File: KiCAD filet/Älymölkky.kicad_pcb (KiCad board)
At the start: 2 copper layers, 99 parts, among them P0.18_TP1 Conn_01x01_Male, U1 nRF52810-QCxx, X1 32MHz Crystal, X1_C1 12pF, X1_C2 12pF, X2 32.768 kHz Crystal, X2_C11 12pF, X2_C12 12pF

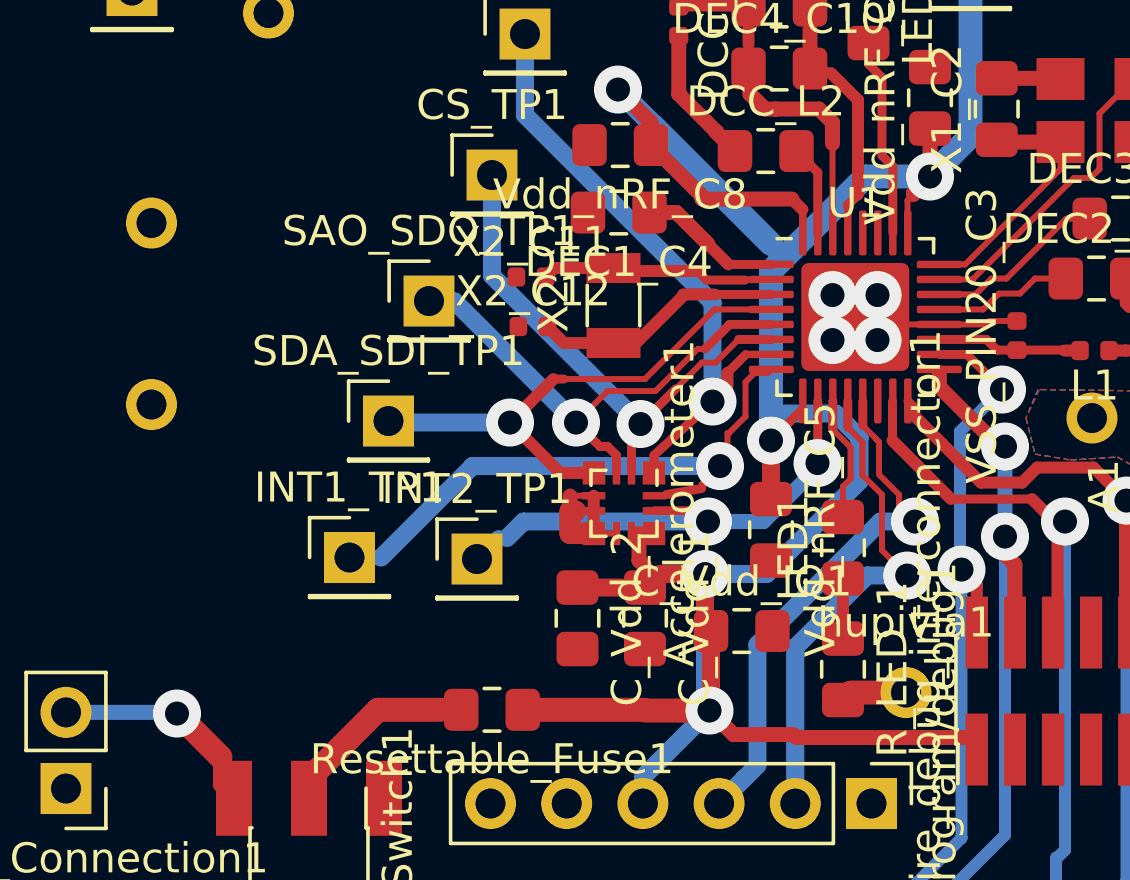
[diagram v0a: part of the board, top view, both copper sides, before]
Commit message: Modified some traces, larger size capacitors on crystal
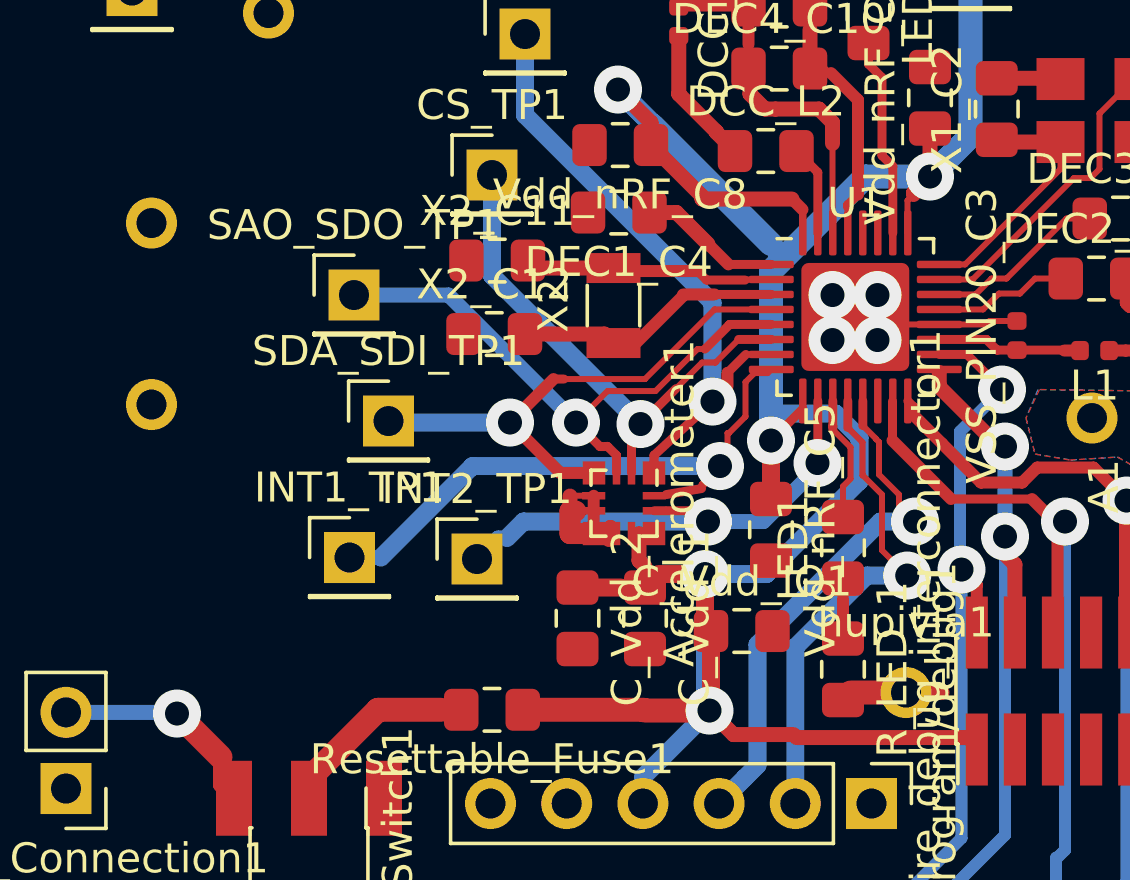
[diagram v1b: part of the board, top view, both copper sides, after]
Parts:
- X2_C11, X2_C12: footprint Capacitor_SMD:C_0402_1005Metric -> Capacitor_SMD:C_0805_2012Metric_Pad1.15x1.40mm_HandSolder
- moved SAO_SDO_TP1 2.51 mm to (114.1, 93.2)
- moved X2_C12 1.31 mm to (118.8, 94.5)
- moved X2_C11 1.25 mm to (118.9, 92.1)
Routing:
- net /~SAO_SDO: track 17.1 -> 19.6 mm
- net Earth: track 34.4 -> 36.6 mm
- net Net-(U1-Pad3): track 8.18 -> 8.83 mm
- net Net-(U1-Pad2): track 7.53 -> 8.10 mm
